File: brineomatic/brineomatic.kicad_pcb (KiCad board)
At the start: 4 copper layers, 106 x 68.5 mm, 169 parts, among them J11 3.5MM, J13 3.5MM, J15 3.5MM, J18 USB_TYPE_C_16PIN, J20 Conn_01x04, J3 THERM, J5 SERVOS, J6 3.5MM, J9 5.08MM, Q1 AO3400A, Q2 AO3400A, Q3 20N06, Q4 AO3400A, Q5 AO3400A, Q6 AO3400A, Q7 FDC6330L, Q8 S8050, Q9 S8050, SW1 RESET, SW2 BOOT, U1 ADS1115IDGSR, U2 LM74700, U3 XL1509-5.0, U4 ESP32-S3-WROOM-1-N16R8, U5 USBLC6-2SC6, U6 XC6210B332MR, U7 CH334F, U8 CH343P, U9 TMC2209-LA, Y1 12Mhz, Y2 32.768kHz

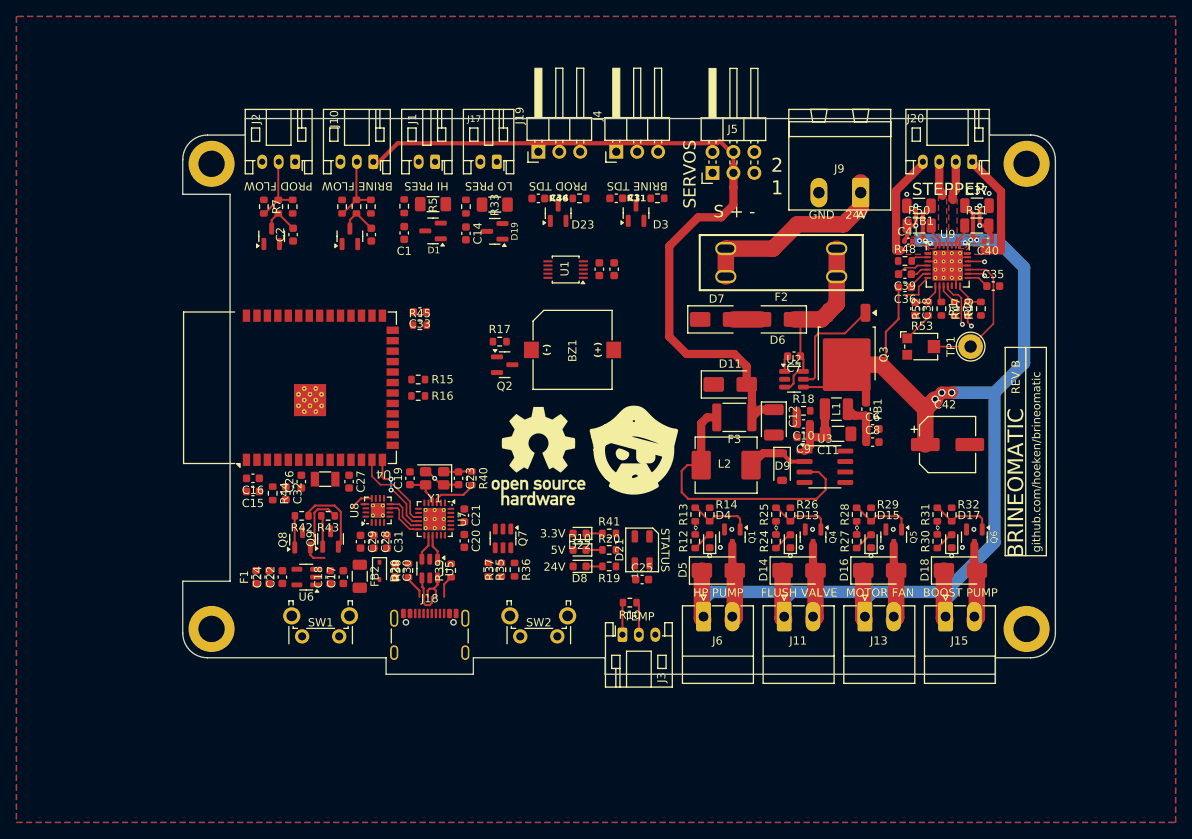
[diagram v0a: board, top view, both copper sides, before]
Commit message: fully routed and erc/drc passed
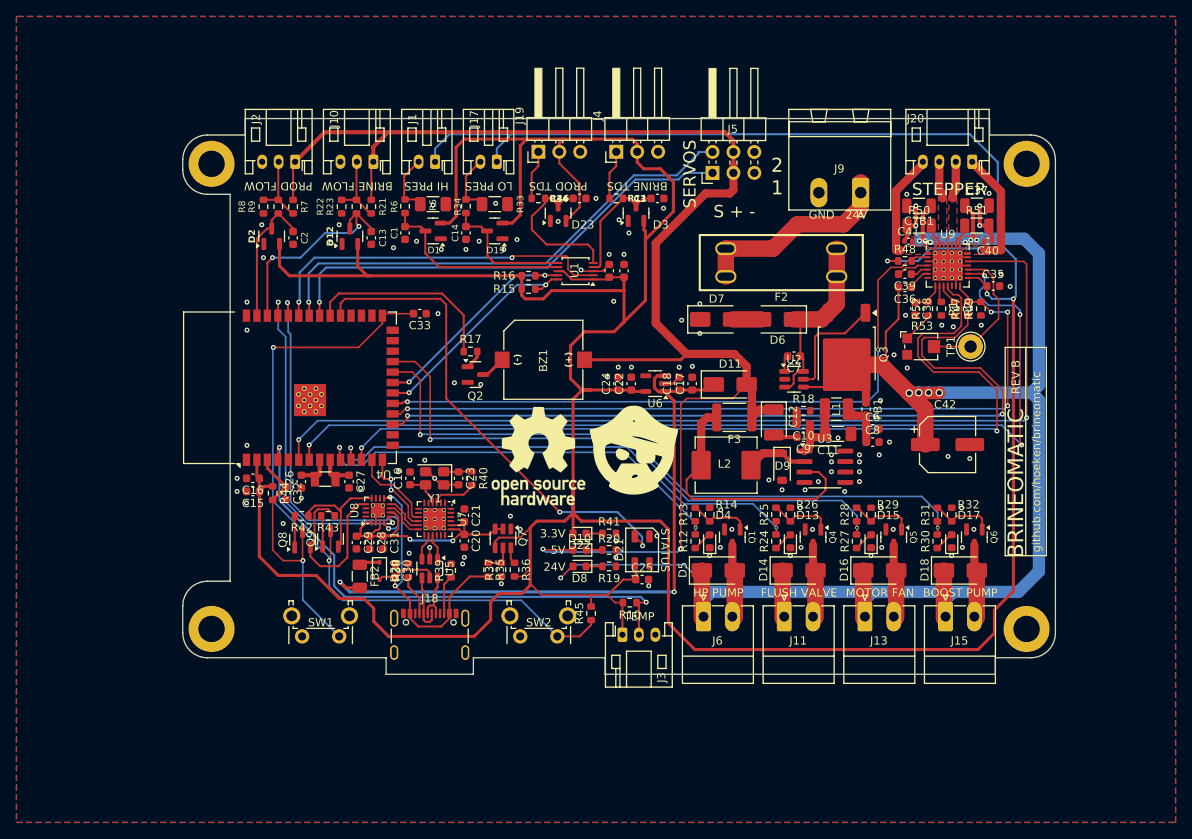
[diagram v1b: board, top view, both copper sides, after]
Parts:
- removed F1: 1A / 3.3v, Fuse:Fuse_0603_1608Metric
- U4: footprint RF_Module:ESP32-S3-WROOM-1 -> yarrboard:ESP32-S3-WROOM-1
- U7: footprint Package_DFN_QFN:QFN-24-1EP_4x4mm_P0.5mm_EP2.7x2.7mm_ThermalVias -> yarrboard:QFN-24-1EP_4x4mm_P0.5mm_EP2.7x2.7mm_ThermalVias
- U8: footprint Package_DFN_QFN:QFN-16-1EP_3x3mm_P0.5mm_EP1.7x1.7mm_ThermalVias -> yarrboard:QFN-16-1EP_3x3mm_P0.5mm_EP1.7x1.7mm_ThermalVias
- moved C17 48.5 mm to (124.9, 59.2)
- moved C18 48.5 mm to (123.3, 59.2)
- moved C22 48.5 mm to (117.5, 59.2)
- moved C24 48.5 mm to (115.9, 59.2)
- moved U6 48.5 mm to (120.4, 59.2)
- moved R45 40.7 mm to (112.6, 87.1), turned to 90 degrees
- moved R16 19.8 mm to (105.0, 46.1), turned to 180 degrees
- moved R15 17.3 mm to (105.0, 47.7), turned to 180 degrees
- moved C3 5.00 mm to (120.7, 36.7), turned to 0 degrees
- moved R11 5.00 mm to (115.7, 36.7), turned to 0 degrees
- moved C34 5.00 mm to (111.2, 36.7), turned to 0 degrees
- moved R46 5.00 mm to (106.2, 36.7), turned to 0 degrees
- moved Q2 3.75 mm to (98.5, 58.1)
- moved BZ1 3.75 mm to (106.8, 56.3)
- moved R17 3.75 mm to (98.0, 55.3)
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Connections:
- net /ESP_RX0 renamed /ESP32-S3/ESP_RXD0
- net /ESP_TX0 renamed /ESP32-S3/ESP_TXD0
- net /ESP_USB+ renamed /ESP32-S3/ESP_USB+
- net /ESP_USB- renamed /ESP32-S3/ESP_USB-
- net /GPIO0 renamed /ESP32-S3/GPIO0_BOOT
- net /GPIO15 renamed /ESP32-S3/GPIO15_RTC
- net /GPIO16 renamed /ESP32-S3/GPIO16_RTC
- net /GPIO3 renamed /ESP32-S3/GPIO3
- net /GPIO35 renamed /ESP32-S3/GPIO35
- net /GPIO36 renamed /ESP32-S3/GPIO36
- net /GPIO37 renamed /ESP32-S3/GPIO37
- net /GPIO45 renamed /ESP32-S3/GPIO45
- net /GPIO46 renamed /ESP32-S3/GPIO46
- C15 pad 1: /ESP32-S3/3.3V -> +3.3V
- C16 pad 1: /ESP32-S3/3.3V -> +3.3V
- C2 pad 1: /ESP32-S3/GPIO5 -> /ESP32-S3/GPIO1
- C22 pad 1: /ESP32-S3/3.3V -> +3.3V
- C24 pad 1: /ESP32-S3/3.3V -> +3.3V
- C25 pad 1: /ESP32-S3/3.3V -> +3.3V
- D2 pad 3: /ESP32-S3/GPIO5 -> /ESP32-S3/GPIO1
- D21 pad 1: /ESP32-S3/3.3V -> +3.3V
- D22 pad 2: /ESP32-S3/3.3V -> +3.3V
- J3 pad 2: /ESP32-S3/GPIO1 -> /ESP32-S3/GPIO4
- J5 pad 1: /ESP32-S3/GPIO18 -> /ESP32-S3/GPIO40
- J5 pad 2: /ESP32-S3/GPIO21 -> /ESP32-S3/GPIO41
- Q7 pad 4: /ESP32-S3/3.3V -> +3.3V
- R10 pad 1: /ESP32-S3/GPIO1 -> /ESP32-S3/GPIO4
- R12 pad 2: /GPIO42 -> SOLENOID1
- R13 pad 1: /GPIO42 -> SOLENOID1
- R17 pad 2: /ESP32-S3/GPIO17 -> /ESP32-S3/GPIO39
- R24 pad 2: /GPIO41 -> SOLENOID2
- R25 pad 1: /GPIO41 -> SOLENOID2
- R27 pad 2: /GPIO40 -> SOLENOID3
- R28 pad 1: /GPIO40 -> SOLENOID3
- R30 pad 2: /GPIO39 -> SOLENOID4
- R31 pad 1: /GPIO39 -> SOLENOID4
- R36 pad 2: /ESP32-S3/3.3V -> +3.3V
- R44 pad 1: /ESP32-S3/3.3V -> +3.3V
- R45 pad 2: /ESP32-S3/3.3V -> +3.3V
- R9 pad 2: /ESP32-S3/GPIO5 -> /ESP32-S3/GPIO1
- U4 pad 10: /ESP32-S3/GPIO17 -> SOLENOID1
- U4 pad 11: /ESP32-S3/GPIO18 -> SOLENOID2
- U4 pad 17: TMC2209_EN -> TMC2209_RX
- U4 pad 18: TMC2209_RX -> TMC2209_TX
- U4 pad 19: TMC2209_TX -> TMC2209_EN
- U4 pad 2: /ESP32-S3/3.3V -> +3.3V
- U4 pad 20: SDA -> SCL
- U4 pad 21: SCL -> SDA
- U4 pad 22: /ESP32-S3/GPIO14 -> SOLENOID4
- U4 pad 23: /ESP32-S3/GPIO21 -> SOLENOID3
- U4 pad 32: /GPIO39 -> /ESP32-S3/GPIO39
- U4 pad 33: /GPIO40 -> /ESP32-S3/GPIO40
- U4 pad 34: /GPIO41 -> /ESP32-S3/GPIO41
- U4 pad 35: /GPIO42 -> ADC_ALERT/RDY
- U4 pad 38: ADC_ALERT/RDY -> /Brine Flowmeter/OUTPUT
- U4 pad 4: /Brine Flowmeter/OUTPUT -> /ESP32-S3/GPIO4
- U6 pad 5: /ESP32-S3/3.3V -> +3.3V
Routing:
- net +3.3V: track 6.65 -> 433.3 mm, vias 0 -> 3
- net +24V: track 182.3 -> 298.9 mm, vias 9 -> 11
- net TMC2209_DIR: track 2.05 -> 117.9 mm, vias 1 -> 2
- net TMC2209_STEP: track 2.13 -> 117.2 mm, vias 1 -> 4
- net TMC2209_DIAG: track 5.81 -> 110.0 mm, vias 1 -> 2
- net TMC2209_RX: track 1.46 -> 98.6 mm, vias 1 -> 2
- net TMC2209_TX: track 3.96 -> 94.2 mm, vias 0 -> 4
- net /ESP32-S3/GPIO0_BOOT: track 0.00 -> 90.0 mm, vias 0 -> 2
- net +5V: track 93.2 -> 178.6 mm, vias 0 -> 2
- net SOLENOID4: track 0.00 -> 80.6 mm, vias 0 -> 2
- net TMC2209_EN: track 2.11 -> 80.2 mm, vias 0 -> 2
- net ESP32_5V: track 0.00 -> 77.6 mm, vias 0 -> 2
- net SOLENOID3: track 0.00 -> 71.8 mm, vias 0 -> 2
- net /ESP32-S3/GPIO4: track 0.00 -> 65.1 mm, vias 0 -> 2
- net SOLENOID2: track 0.00 -> 60.7 mm, vias 0 -> 2
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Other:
- board size 106 x 68.5 mm -> 106 x 67.5 mm

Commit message: removed the onboard fuse.
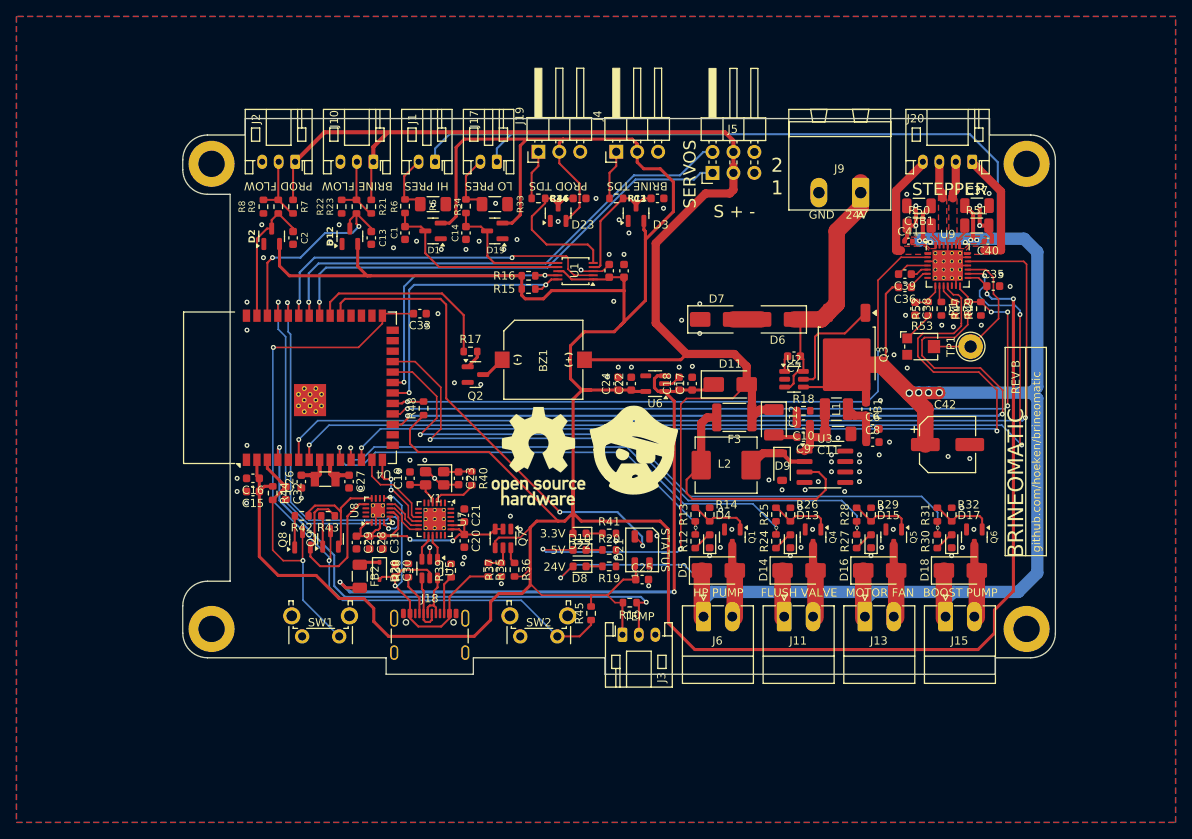
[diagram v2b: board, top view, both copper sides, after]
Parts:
- removed F2: 10A, yarrboard:FUSE-TH_XF-508P-A-B
- moved R48 61.2 mm to (92.2, 62.2), turned to 90 degrees
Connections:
- J9 pad 1: Net-(J9-Pin_1) -> Net-(D6-A1)
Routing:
- net Net-(J9-Pin_1): track 24.9 -> 0.00 mm
- net Net-(D6-A1): track 22.0 -> 31.3 mm
- net SCL: track 27.3 -> 34.6 mm
- net SDA: track 26.6 -> 33.4 mm
- net +3.3V: track 433.3 -> 436.3 mm, vias 3 -> 2
- net TMC2209_EN: track 80.2 -> 82.2 mm
- net SOLENOID4: track 80.6 -> 82.3 mm
- net SOLENOID3: track 71.8 -> 72.9 mm
- net GND: vias 105 -> 106

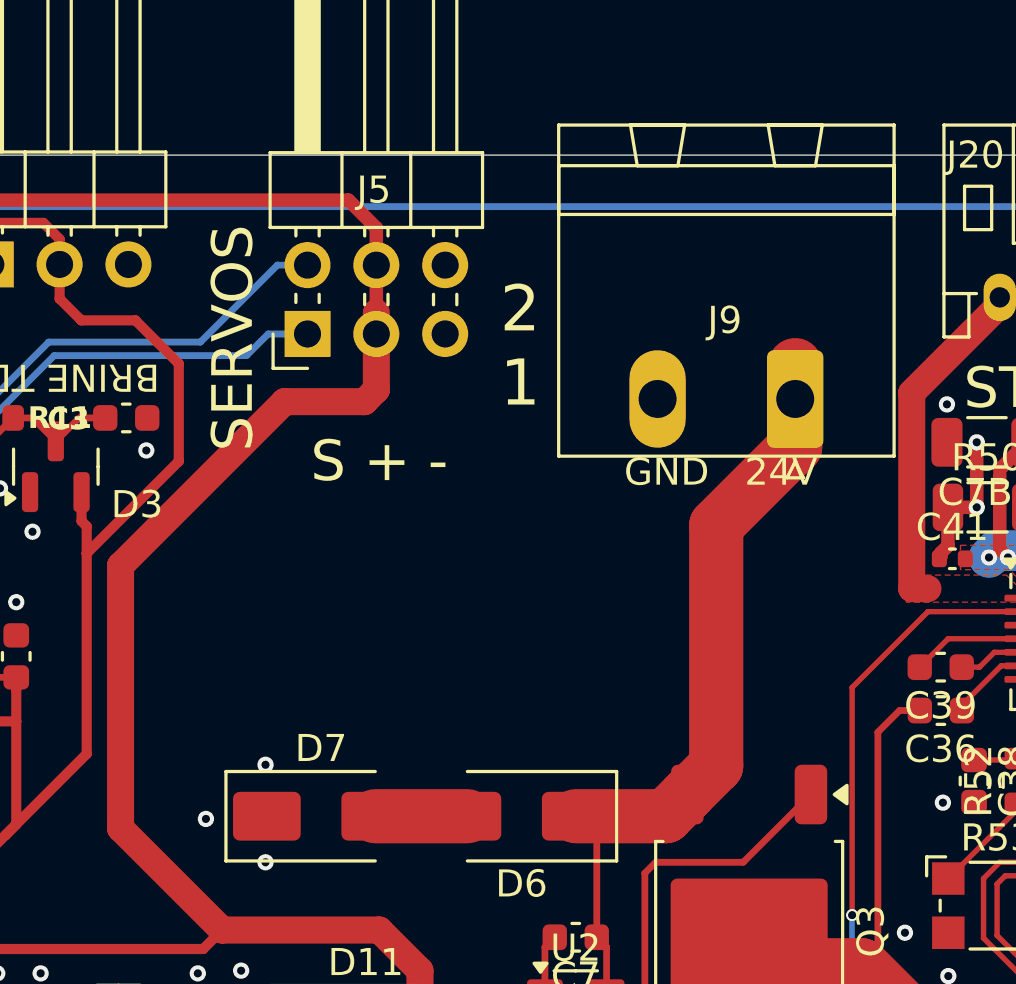
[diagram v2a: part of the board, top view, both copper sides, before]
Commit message: re-added fuse, switched to 5x20mm
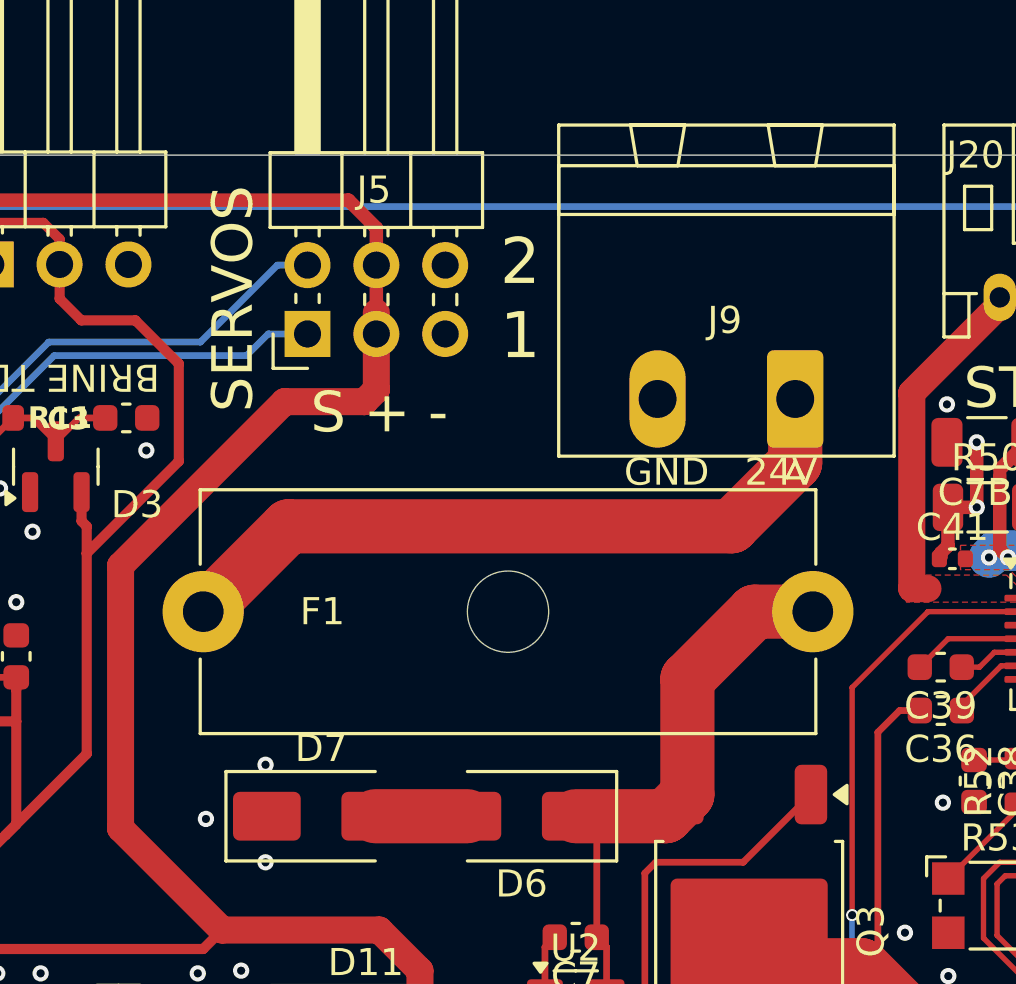
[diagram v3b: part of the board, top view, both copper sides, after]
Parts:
- added F1: 1A / 5x20mm, yarrboard:Fuseholder_Cylinder-5x20mm_LittelFuse_646, F.Cu at (123.5, 43.9)
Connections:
- J9 pad 1: Net-(D6-A1) -> Net-(J9-Pin_1)
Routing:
- net Net-(J9-Pin_1): track 0.00 -> 26.5 mm
- net Net-(D6-A1): track 31.3 -> 23.7 mm

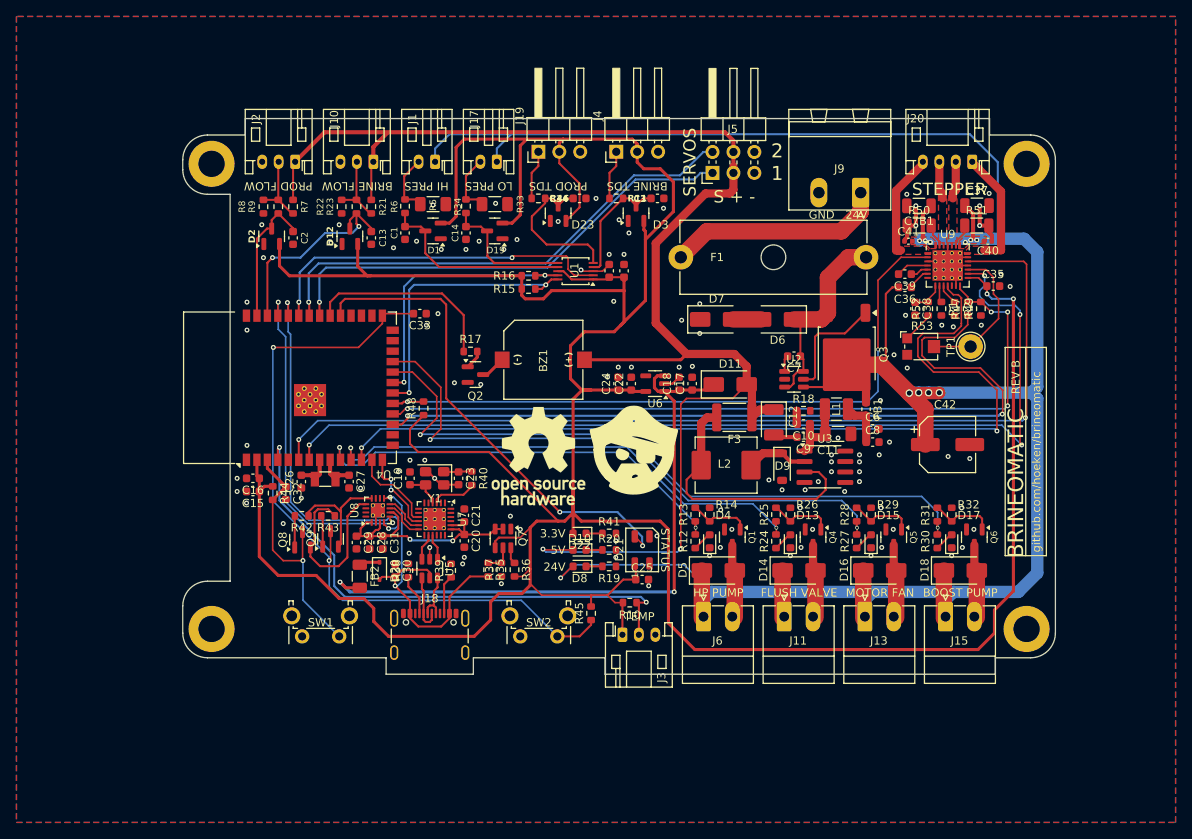
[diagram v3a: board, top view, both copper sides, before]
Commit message: silkscreen good and all drc errors fixed.
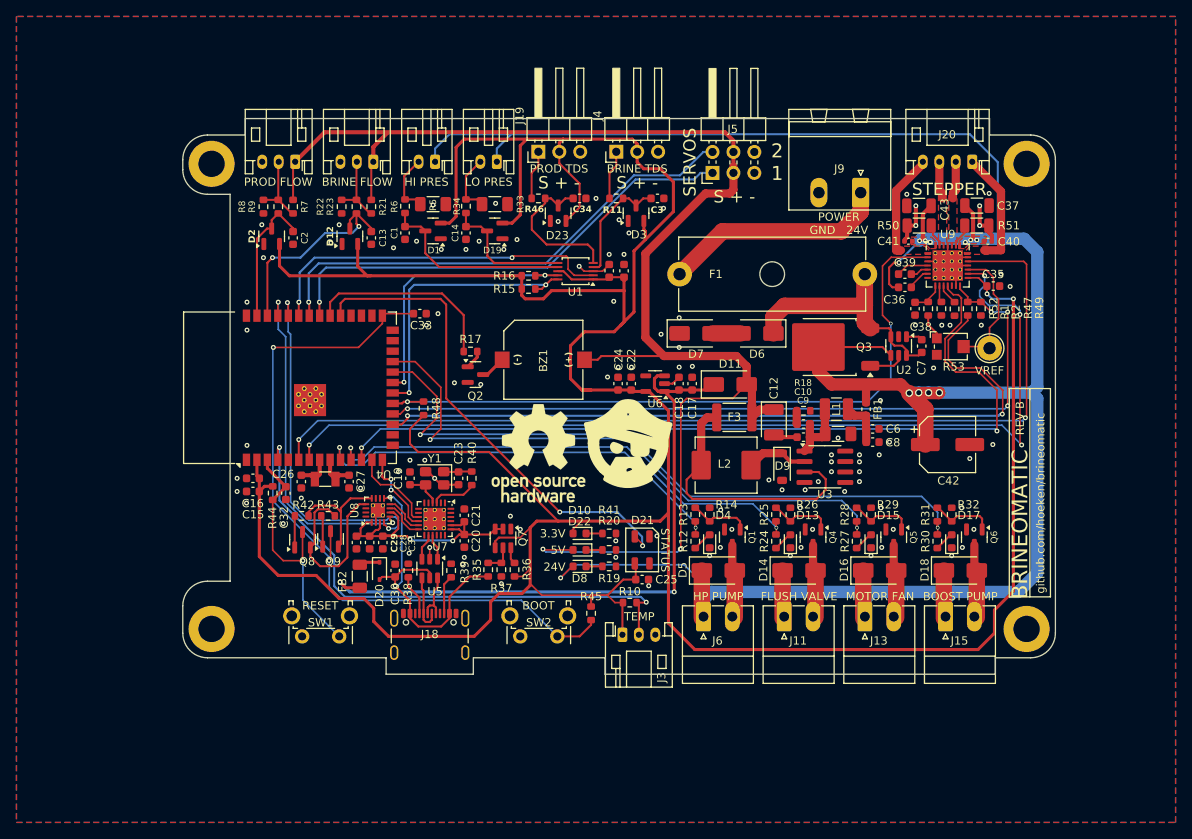
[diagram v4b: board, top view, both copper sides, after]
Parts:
- F1: value 1A / 5x20mm -> 3A / 5x20mm
- J11, J13, J15, J6: footprint Connector_Phoenix_MC:PhoenixContact_MC_1,5_2-G-3.5_1x02_P3.50mm_Horizontal -> yarrboard:PhoenixContact_MC_1,5_2-G-3.5_1x02_P3.50mm_Horizontal
- J9: footprint Connector_Phoenix_MSTB:PhoenixContact_MSTBA_2,5_2-G-5,08_1x02_P5.08mm_Horizontal -> yarrboard:PhoenixContact_MSTBA_2,5_2-G-5,08_1x02_P5.08mm_Horizontal
- moved C7 15.6 mm to (152.8, 54.6), turned to 90 degrees
- moved U2 13.3 mm to (150.0, 54.6), turned to -90 degrees
- moved R53 3.60 mm to (156.4, 54.7)
- moved D6 3.02 mm to (132.8, 53.1)
- moved D7 3.02 mm to (125.3, 53.1)
- moved Q3 2.35 mm to (141.5, 54.8), turned to 180 degrees
- moved TP1 2.31 mm to (161.0, 54.9)
- moved F1 2.06 mm to (123.3, 45.9)
- moved SYM2 1.06 mm to (117.1, 66.5)
- moved SYM1 0.35 mm to (106.2, 67.7)
- renumbered C7B1 to C43
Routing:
- net +24V: track 299.0 -> 309.5 mm, vias 11 -> 12
- net Net-(D6-A1): track 23.7 -> 33.4 mm
- net Net-(Q3-G): track 13.8 -> 4.36 mm
- net TMC2209_DIAG: track 110.0 -> 103.5 mm
- net TMC2209_RX: track 98.6 -> 92.2 mm
- net /Stepper Driver/VREF: track 18.0 -> 15.8 mm
- net +3.3V: track 436.3 -> 434.4 mm
- net TMC2209_EN: track 82.2 -> 83.7 mm
- net Net-(J9-Pin_1): track 26.5 -> 27.5 mm
- net GND: track 33.4 -> 33.8 mm, vias 106 -> 105
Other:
- board text added: "BOOT"
- board text added: "POWER GND 24V"
- board text added: "RESET"
- board text added: "VREF"
- board text removed: "GND 24V"

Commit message: worked on bom for rev b prototype run
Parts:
- C35, C36, C40, C41: value 100n/50V -> 100nF/50v
- C37, C43: value 10u/35V -> 10uF/35v
- C38: value 4.7u/6.3v -> 4.7uF/6.3v
- C39: value 22n/50V -> 22nF/50v
- D10, D8: value PWR -> RED
- D13, D15, D17, D22, D4: value LED -> RED
- J3: value THERM -> ~
- J5: value SERVOS -> ~
- R35: value 100 -> 100R

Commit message: updated jlc parts rotations and placement offsets
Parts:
- C10: value 4.7uF/50v -> 4.7uF / 50v
- C11, C37, C43: value 10uF/35v -> 10uF / 35v
- C35, C36, C40, C41: value 100nF/50v -> 100nF / 50v
- C38: value 4.7uF/6.3v -> 4.7uF / 6.3v
- C39: value 22nF/50v -> 22nF / 50v
- C42: value 100uF 35v -> 100uF / 35v
- C8: value 470nF/50v -> 470nF / 50v
